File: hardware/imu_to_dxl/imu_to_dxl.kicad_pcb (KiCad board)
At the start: 2 copper layers, 27.1 x 30.2 mm, 74 parts, among them J1 1.8mm螺丝孔, J2 1.8mm螺丝孔, J3 1.8mm螺丝孔, J4 1.8mm螺丝孔, Q1 MMBT3906, U1 ETA2845S2G_C22362741, U2 GD32F303CCT6, U3 LSM6DSV16XTR, U4 SN74LVC1G126DBVR, U5 SN74LVC1G125DBV, U6 ME6211C18M5G-N, X1 XL2EL89CSI-111YLC-12M

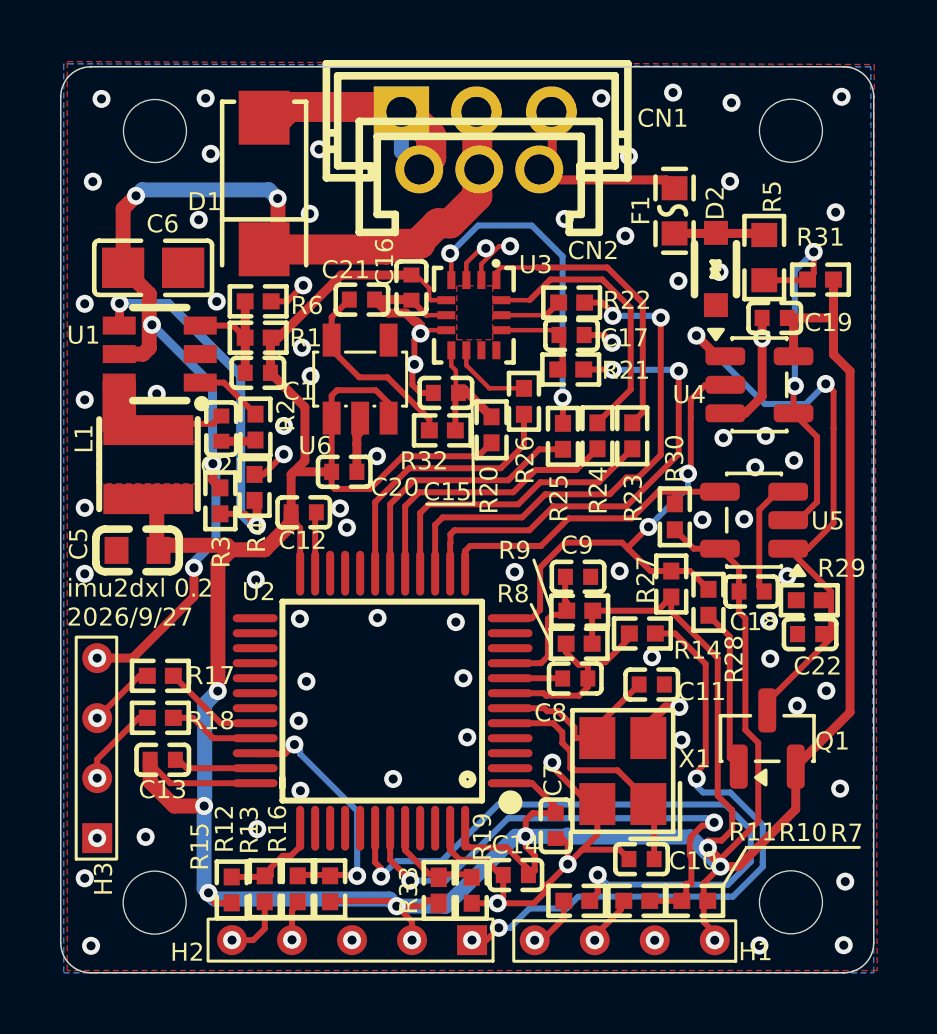
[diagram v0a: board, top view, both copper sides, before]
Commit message: 更新imu_to_dxl:1、优化MCU晶震电路；2、增加调试知识灯
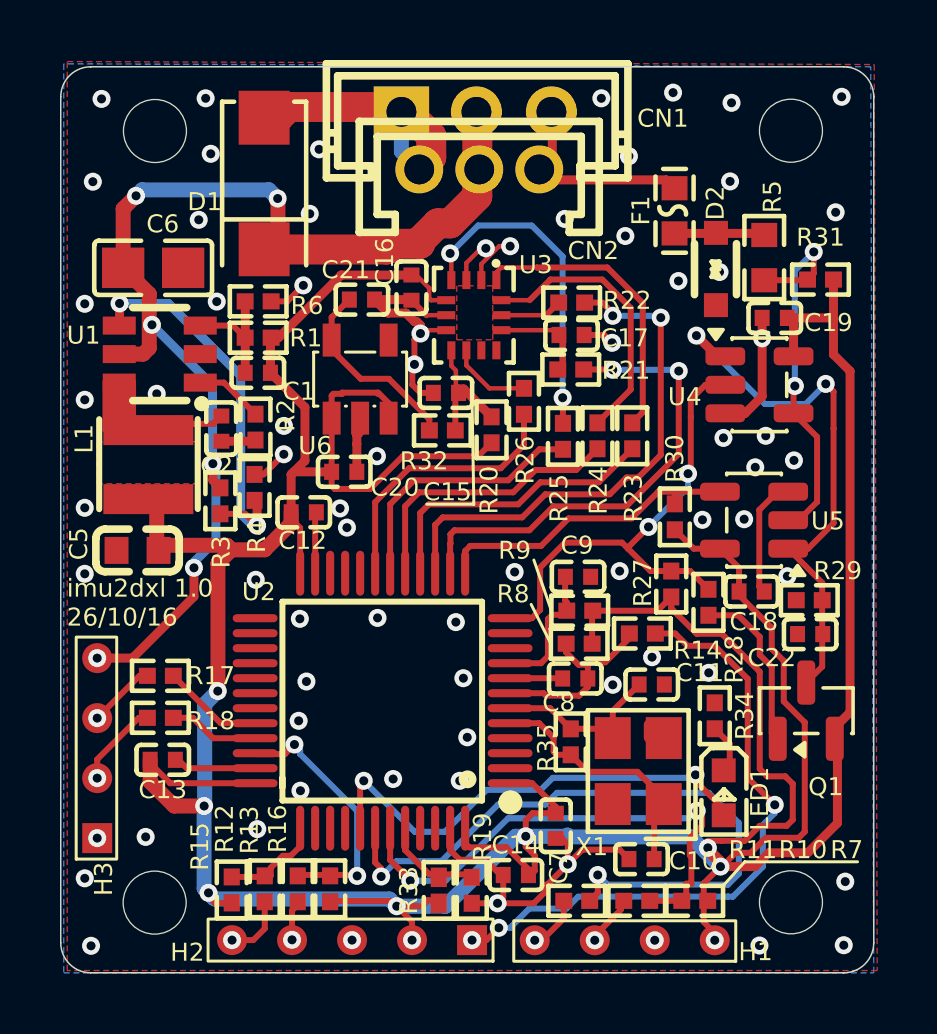
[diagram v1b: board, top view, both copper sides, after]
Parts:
- added LED1: GL0603UG01, microduck:LED0603-RD, F.Cu at (132.1, 143.5)
- added R34: 100K, microduck:R0402, F.Cu at (131.8, 140.9)
- added R35: 1M, microduck:R0402, F.Cu at (127.0, 141.8)
- C10, C11: value 27pF/50V -> 20pF/50V
- CN1: value ~ -> B3B-EH-A(LF)(SN)
- CN2: value ~ -> AMP175778/8283/A2007WV-3P
- D1: value SMAJ24A -> SMAJ36A
- R5: value 51R -> 0R
- moved Q1 1.60 mm to (134.8, 140.8)
- moved X1 0.51 mm to (129.2, 142.8)
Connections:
- U2 pad 41: unconnected-(U2-PB5-Pad41) -> /DEBUG_LED
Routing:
- net /DEBUG_LED: track 0.00 -> 16.0 mm, vias 0 -> 2
- net +3.3V: track 144.5 -> 151.3 mm
- net GND: track 58.0 -> 52.7 mm, vias 78 -> 71
- net /TXD_EN: track 20.3 -> 18.5 mm
- net Net-(LED1-K): track 0.00 -> 1.59 mm
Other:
- board text added: "imu2dxl 1.0 26/10/16"
- board text removed: "imu2dxl 0.2 2026/9/27"
